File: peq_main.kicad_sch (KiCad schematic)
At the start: 39 parts, among them SW1 3PDT_FootSwitch

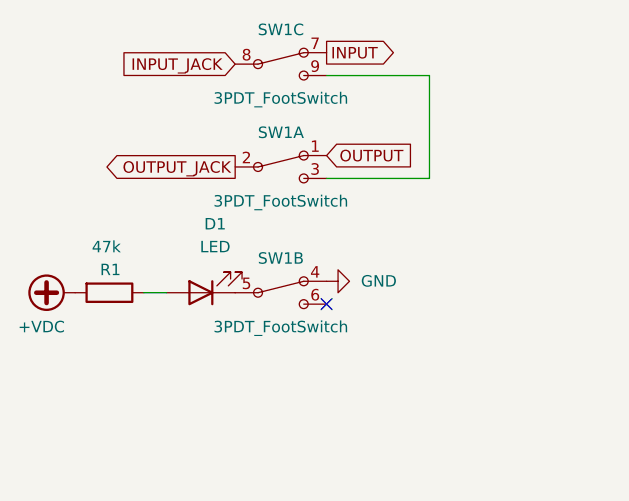
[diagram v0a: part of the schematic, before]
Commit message: add protection components and fix layout
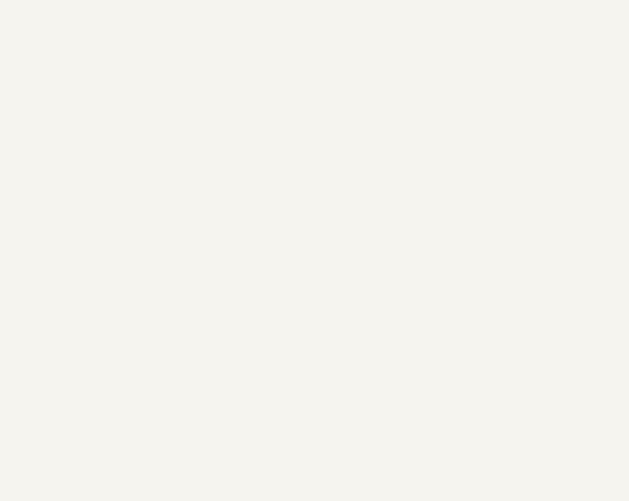
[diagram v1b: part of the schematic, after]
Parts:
- removed D1: LED, LED_THT:LED_D3.0mm, symbol Device:LED
- removed R1: 47k, ak_misc:R_Axial_DIN0207_L6.3mm_D2.5mm_P7.62mm_with_SMD, symbol Device:R
- removed SW1: 3PDT_FootSwitch, ak_misc:3PDT_FootSwitch_ovalpad, symbol ak_misc:3PDT_FootSwitch
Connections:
- no-connect marks 1 -> 0
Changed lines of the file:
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@@
   (junction (at 92.71 179.07) (diameter 0) (color 0 0 0 0)
   )
-  (no_connect (at 54.61 53.34))
   (wire (pts (xy 92.71 113.03) (xy 92.71 120.65))
     (stroke (width 0) (type default) (color 0 0 0 0))
@@
     (stroke (width 0) (type default) (color 0 0 0 0))
   )
-  (wire (pts (xy 66.04 39.37) (xy 54.61 39.37))
-    (stroke (width 0) (type default) (color 0 0 0 0))
-  )
   (wire (pts (xy 242.57 100.33) (xy 248.92 100.33))
     (stroke (width 0) (type default) (color 0 0 0 0))
@@
     (stroke (width 0) (type default) (color 0 0 0 0))
   )
-  (wire (pts (xy 66.04 27.94) (xy 66.04 39.37))
-    (stroke (width 0) (type default) (color 0 0 0 0))
-  )
   (wire (pts (xy 237.49 115.57) (xy 242.57 115.57))
     (stroke (width 0) (type default) (color 0 0 0 0))
@@
     (stroke (width 0) (type default) (color 0 0 0 0))
   )
-  (wire (pts (xy 34.29 52.07) (xy 36.83 52.07))
-    (stroke (width 0) (type default) (color 0 0 0 0))
-  )
   (wire (pts (xy 92.71 166.37) (xy 92.71 172.72))
     (stroke (width 0) (type default) (color 0 0 0 0))
@@
     (stroke (width 0) (type default) (color 0 0 0 0))
   )
-  (wire (pts (xy 54.61 27.94) (xy 66.04 27.94))
-    (stroke (width 0) (type default) (color 0 0 0 0))
-  )
   (wire (pts (xy 92.71 179.07) (xy 92.71 185.42))
     (stroke (width 0) (type default) (color 0 0 0 0))
@@
     (effects (font (size 1.27 1.27)) (justify left bottom))
   )
-  (global_label "INPUT" (shape output) (at 54.61 25.4 0) (fields_autoplaced)
-    (effects (font (size 1.27 1.27)) (justify left))
-    (property "Intersheet References" "${INTERSHEET_REFS}" (id 0) (at 62.5264 25.3206 0)
-      (effects (font (size 1.27 1.27)) (justify left) hide)
-    )
-  )
   (global_label "SW3D" (shape bidirectional) (at 76.2 127 180) (fields_autoplaced)
     (effects (font (size 1.27 1.27)) (justify right))
@@
     (effects (font (size 1.27 1.27)) (justify right))
     (property "Intersheet References" "${INTERSHEET_REFS}" (id 0) (at 219.7159 138.3506 0)
-      (effects (font (size 1.27 1.27)) (justify right) hide)
-    )
-  )
-  (global_label "INPUT_JACK" (shape input) (at 44.45 26.67 180) (fields_autoplaced)
-    (effects (font (size 1.27 1.27)) (justify right))
-    (property "Intersheet References" "${INTERSHEET_REFS}" (id 0) (at 30.9698 26.5906 0)
       (effects (font (size 1.27 1.27)) (justify right) hide)
     )
@@
     )
   )
-  (global_label "OUTPUT" (shape input) (at 54.61 36.83 0) (fields_autoplaced)
-    (effects (font (size 1.27 1.27)) (justify left))
-    (property "Intersheet References" "${INTERSHEET_REFS}" (id 0) (at 64.2198 36.9094 0)
-      (effects (font (size 1.27 1.27)) (justify left) hide)
-    )
-  )
   (global_label "SW2I" (shape bidirectional) (at 227.33 153.67 180) (fields_autoplaced)
     (effects (font (size 1.27 1.27)) (justify right))
@@
     )
   )
-  (global_label "OUTPUT_JACK" (shape output) (at 44.45 38.1 180) (fields_autoplaced)
-    (effects (font (size 1.27 1.27)) (justify right))
-    (property "Intersheet References" "${INTERSHEET_REFS}" (id 0) (at 29.2764 38.0206 0)
-      (effects (font (size 1.27 1.27)) (justify right) hide)
-    )
-  )
   (symbol (lib_id "Device:C") (at 233.68 100.33 90) (unit 1)
     (in_bom yes) (on_board yes)
@@
     (pin "2")
   )
-  (symbol (lib_id "ak_misc:3PDT_FootSwitch") (at 49.53 26.67 0) (unit 3)
-    (in_bom yes) (on_board yes)
-    (property "Reference" "SW1" (id 0) (at 49.53 22.86 0))
-    (property "Value" "3PDT_FootSwitch" (id 1) (at 49.53 30.48 0))
-    (property "Footprint" "ak_misc:3PDT_FootSwitch_ovalpad" (id 2) (at 49.53 26.67 0)
-      (effects (font (size 1.27 1.27)) hide)
-    )
-    (property "Datasheet" "" (id 3) (at 49.53 26.67 0)
-      (effects (font (size 1.27 1.27)) hide)
-    )
-    (pin "1")
-    (pin "2")
-    (pin "3")
-    (pin "4")
-    (pin "5")
-    (pin "6")
-    (pin "7")
-    (pin "8")
-    (pin "9")
-  )
   (symbol (lib_id "Device:C") (at 82.55 139.7 90) (unit 1)
     (in_bom yes) (on_board yes)
@@
     (pin "2")
   )
-  (symbol (lib_id "ak_misc:3PDT_FootSwitch") (at 49.53 52.07 0) (unit 2)
-    (in_bom yes) (on_board yes)
-    (property "Reference" "SW1" (id 0) (at 49.53 48.26 0))
-    (property "Value" "3PDT_FootSwitch" (id 1) (at 49.53 55.88 0))
-    (property "Footprint" "ak_misc:3PDT_FootSwitch_ovalpad" (id 2) (at 49.53 52.07 0)
-      (effects (font (size 1.27 1.27)) hide)
-    )
-    (property "Datasheet" "" (id 3) (at 49.53 52.07 0)
-      (effects (font (size 1.27 1.27)) hide)
-    )
-    (pin "1")
-    (pin "2")
-    (pin "3")
-    (pin "4")
-    (pin "5")
-    (pin "6")
-    (pin "7")
-    (pin "8")
-    (pin "9")
-  )
   (symbol (lib_id "Device:C") (at 233.68 69.85 90) (unit 1)
     (in_bom yes) (on_board yes)
@@
     (pin "2")
   )
-  (symbol (lib_id "Device:LED") (at 40.64 52.07 180) (unit 1)
-    (in_bom yes) (on_board yes) (fields_autoplaced)
-    (property "Reference" "D1" (id 0) (at 42.2275 44.45 0))
-    (property "Value" "LED" (id 1) (at 42.2275 46.99 0))
-    (property "Footprint" "LED_THT:LED_D3.0mm" (id 2) (at 40.64 52.07 0)
-      (effects (font (size 1.27 1.27)) hide)
-    )
-    (property "Datasheet" "~" (id 3) (at 40.64 52.07 0)
-      (effects (font (size 1.27 1.27)) hide)
-    )
-    (pin "1")
-    (pin "2")
-  )
   (symbol (lib_id "Device:C") (at 233.68 153.67 90) (unit 1)
     (in_bom yes) (on_board yes)
@@
     (pin "2")
   )
-  (symbol (lib_id "Device:R") (at 30.48 52.07 270) (unit 1)
-    (in_bom yes) (on_board yes)
-    (property "Reference" "R1" (id 0) (at 31.75 49.5301 90)
-      (effects (font (size 1.27 1.27)) (justify right))
-    )
-    (property "Value" "47k" (id 1) (at 31.75 46.9901 90)
-      (effects (font (size 1.27 1.27)) (justify right))
-    )
-    (property "Footprint" "ak_misc:R_Axial_DIN0207_L6.3mm_D2.5mm_P7.62mm_with_SMD" (id 2) (at 30.48 50.292 90)
-      (effects (font (size 1.27 1.27)) hide)
-    )
-    (property "Datasheet" "~" (id 3) (at 30.48 52.07 0)
-      (effects (font (size 1.27 1.27)) hide)
-    )
-    (pin "1")
-    (pin "2")
-  )
   (symbol (lib_id "Device:C") (at 82.55 120.65 90) (unit 1)
     (in_bom yes) (on_board yes)
@@
     (pin "2")
   )
-  (symbol (lib_id "power:GND") (at 54.61 50.8 90) (unit 1)
-    (in_bom yes) (on_board yes) (fields_autoplaced)
-    (property "Reference" "#PWR0102" (id 0) (at 60.96 50.8 0)
-      (effects (font (size 1.27 1.27)) hide)
-    )
-    (property "Value" "GND" (id 1) (at 58.42 50.7999 90)
-      (effects (font (size 1.27 1.27)) (justify right))
-    )
-    (property "Footprint" "" (id 2) (at 54.61 50.8 0)
-      (effects (font (size 1.27 1.27)) hide)
-    )
-    (property "Datasheet" "" (id 3) (at 54.61 50.8 0)
-      (effects (font (size 1.27 1.27)) hide)
-    )
-    (pin "1")
-  )
   (symbol (lib_id "Device:L") (at 248.92 104.14 180) (unit 1)
     (in_bom yes) (on_board yes)
@@
     (pin "2")
   )
-  (symbol (lib_id "ak_misc:3PDT_FootSwitch") (at 49.53 38.1 0) (unit 1)
-    (in_bom yes) (on_board yes)
-    (property "Reference" "SW1" (id 0) (at 49.53 34.29 0))
-    (property "Value" "3PDT_FootSwitch" (id 1) (at 49.53 41.91 0))
-    (property "Footprint" "ak_misc:3PDT_FootSwitch_ovalpad" (id 2) (at 49.53 38.1 0)
-      (effects (font (size 1.27 1.27)) hide)
-    )
-    (property "Datasheet" "" (id 3) (at 49.53 38.1 0)
-      (effects (font (size 1.27 1.27)) hide)
-    )
-    (pin "1")
-    (pin "2")
-    (pin "3")
-    (pin "4")
-    (pin "5")
-    (pin "6")
-    (pin "7")
-    (pin "8")
-    (pin "9")
-  )
-  (symbol (lib_id "power:+VDC") (at 26.67 52.07 90) (unit 1)
-    (in_bom yes) (on_board yes)
-    (property "Reference" "#PWR01" (id 0) (at 29.21 52.07 0)
-      (effects (font (size 1.27 1.27)) hide)
-    )
-    (property "Value" "+VDC" (id 1) (at 20.32 55.88 90)
-      (effects (font (size 1.27 1.27)) (justify right))
-    )
-    (property "Footprint" "" (id 2) (at 26.67 52.07 0)
-      (effects (font (size 1.27 1.27)) hide)
-    )
-    (property "Datasheet" "" (id 3) (at 26.67 52.07 0)
-      (effects (font (size 1.27 1.27)) hide)
-    )
-    (pin "1")
-  )
   (symbol (lib_id "Device:C") (at 82.55 154.94 90) (unit 1)

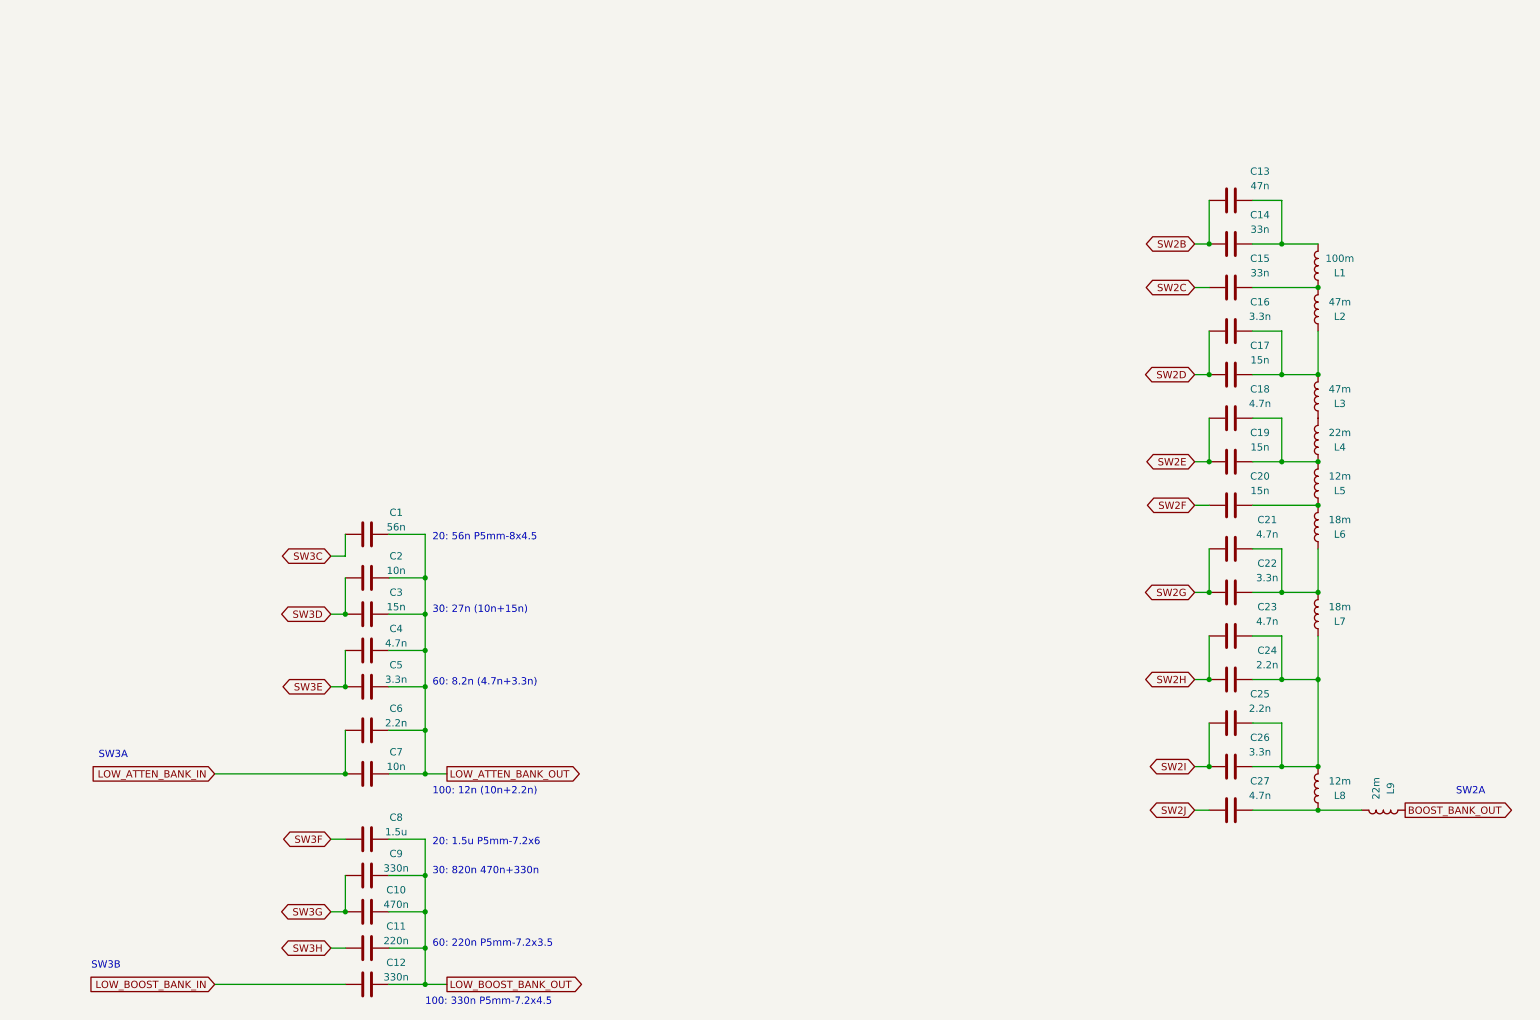
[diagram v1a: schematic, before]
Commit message: update comments and credits
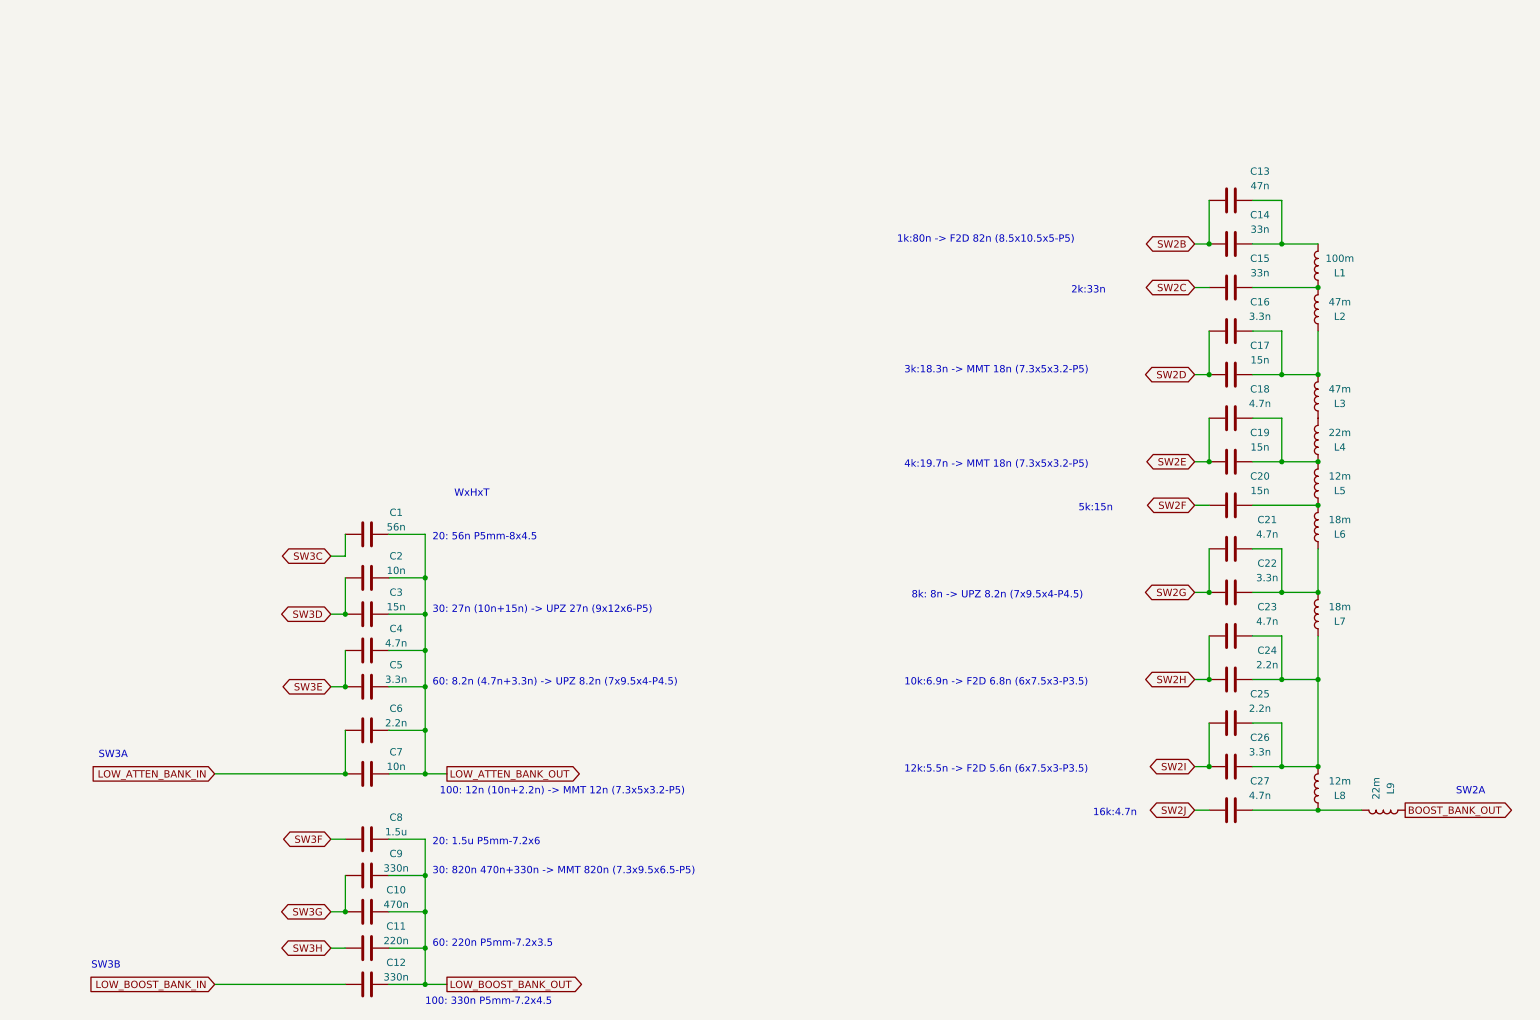
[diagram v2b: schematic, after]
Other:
- note added: "100: 12n (10n+2.2n) -> MMT 12n (7.3x5x3.2-P5)"
- note added: "10k:6.9n -> F2D 6.8n (6x7.5x3-P3.5)"
- note added: "12k:5.5n -> F2D 5.6n (6x7.5x3-P3.5)"
- note added: "16k:4.7n"
- note added: "1k:80n -> F2D 82n (8.5x10.5x5-P5)"
- note added: "2k:33n"
- note added: "30: 27n (10n+15n) -> UPZ 27n (9x12x6-P5)"
- note added: "30: 820n 470n+330n -> MMT 820n (7.3x9.5x6.5-P5)"
- note added: "3k:18.3n -> MMT 18n (7.3x5x3.2-P5)"
- note added: "4k:19.7n -> MMT 18n (7.3x5x3.2-P5)"
- note added: "5k:15n"
- note added: "60: 8.2n (4.7n+3.3n) -> UPZ 8.2n (7x9.5x4-P4.5)"
- note added: "8k: 8n -> UPZ 8.2n (7x9.5x4-P4.5)"
- note added: "WxHxT"
- note removed: "100: 12n (10n+2.2n)"
- note removed: "30: 27n (10n+15n)"
- note removed: "30: 820n 470n+330n"
- note removed: "60: 8.2n (4.7n+3.3n)"
- company: (none) -> MST/mesotokyo
- title: (none) -> PEQ
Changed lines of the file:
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@@
 (kicad_sch (version 20211123) (generator eeschema)
   (paper "A4")
+  (title_block
+    (title "PEQ")
+    (date "2024-11-02")
+    (rev "v1.1")
+    (company "MST/mesotokyo")
+    (comment 1 "https://meso.tokyo/")
+  )
   (junction (at 92.71 185.42) (diameter 0) (color 0 0 0 0)
   )
@@
     (stroke (width 0) (type default) (color 0 0 0 0))
   )
-  (text "30: 820n 470n+330n" (at 93.98 172.72 0)
+  (text "30: 820n 470n+330n -> MMT 820n (7.3x9.5x6.5-P5)" (at 93.98 172.72 0)
     (effects (font (size 1.27 1.27)) (justify left bottom))
   )
@@
     (effects (font (size 1.27 1.27)) (justify left bottom))
   )
-  (text "100: 12n (10n+2.2n)" (at 93.98 158.75 0)
+  (text "5k:15n" (at 207.01 109.22 0)
+    (effects (font (size 1.27 1.27)) (justify left bottom))
+  )
+  (text "100: 12n (10n+2.2n) -> MMT 12n (7.3x5x3.2-P5)" (at 95.25 158.75 0)
+    (effects (font (size 1.27 1.27)) (justify left bottom))
+  )
+  (text "10k:6.9n -> F2D 6.8n (6x7.5x3-P3.5)" (at 176.53 139.7 0)
     (effects (font (size 1.27 1.27)) (justify left bottom))
   )
@@
     (effects (font (size 1.27 1.27)) (justify left bottom))
   )
-  (text "60: 8.2n (4.7n+3.3n)" (at 93.98 139.7 0)
+  (text "4k:19.7n -> MMT 18n (7.3x5x3.2-P5)" (at 176.53 101.6 0)
+    (effects (font (size 1.27 1.27)) (justify left bottom))
+  )
+  (text "WxHxT" (at 97.79 106.68 0)
+    (effects (font (size 1.27 1.27)) (justify left bottom))
+  )
+  (text "60: 8.2n (4.7n+3.3n) -> UPZ 8.2n (7x9.5x4-P4.5)" (at 93.98 139.7 0)
+    (effects (font (size 1.27 1.27)) (justify left bottom))
+  )
+  (text "2k:33n" (at 205.74 71.12 0)
     (effects (font (size 1.27 1.27)) (justify left bottom))
   )
@@
     (effects (font (size 1.27 1.27)) (justify left bottom))
   )
+  (text "8k: 8n -> UPZ 8.2n (7x9.5x4-P4.5)" (at 177.8 124.46 0)
+    (effects (font (size 1.27 1.27)) (justify left bottom))
+  )
+  (text "1k:80n -> F2D 82n (8.5x10.5x5-P5)" (at 175.26 62.23 0)
+    (effects (font (size 1.27 1.27)) (justify left bottom))
+  )
   (text "20: 56n P5mm-8x4.5" (at 93.98 114.3 0)
     (effects (font (size 1.27 1.27)) (justify left bottom))
   )
-  (text "30: 27n (10n+15n)" (at 93.98 127 0)
-    (effects (font (size 1.27 1.27)) (justify left bottom))
-  )
+  (text "30: 27n (10n+15n) -> UPZ 27n (9x12x6-P5)" (at 93.98 127 0)
+    (effects (font (size 1.27 1.27)) (justify left bottom))
+  )
+  (text "16k:4.7n" (at 209.55 162.56 0)
+    (effects (font (size 1.27 1.27)) (justify left bottom))
+  )
+  (text "3k:18.3n -> MMT 18n (7.3x5x3.2-P5)" (at 176.53 85.09 0)
+    (effects (font (size 1.27 1.27)) (justify left bottom))
+  )
+  (text "12k:5.5n -> F2D 5.6n (6x7.5x3-P3.5)" (at 176.53 154.94 0)
+    (effects (font (size 1.27 1.27)) (justify left bottom))
+  )
